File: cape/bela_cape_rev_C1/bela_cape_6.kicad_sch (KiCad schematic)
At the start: 42 parts, among them IC3 ES9080Q, U1 TL974, U2 TL974

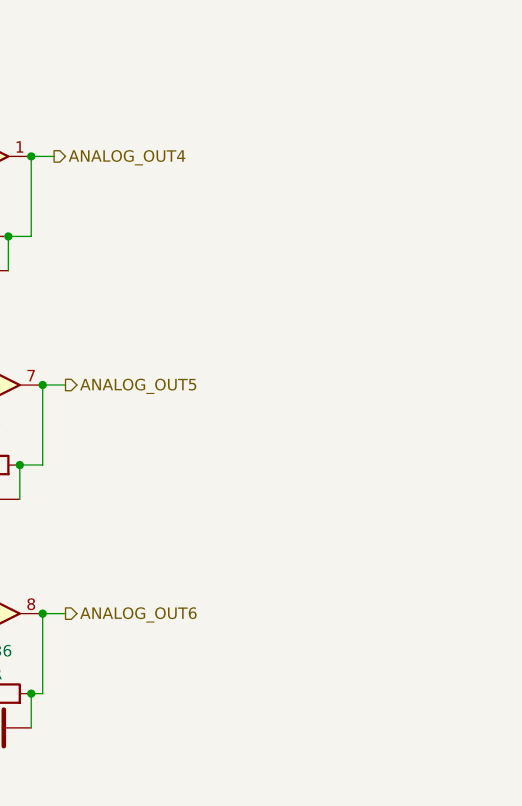
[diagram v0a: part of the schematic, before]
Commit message: Updates to Bela cape C1, adding 3-pin connectors for raw analog out
(cherry picked from commit eb88a9ebe73bf9c3f735ce6d0fd609408781e91a)
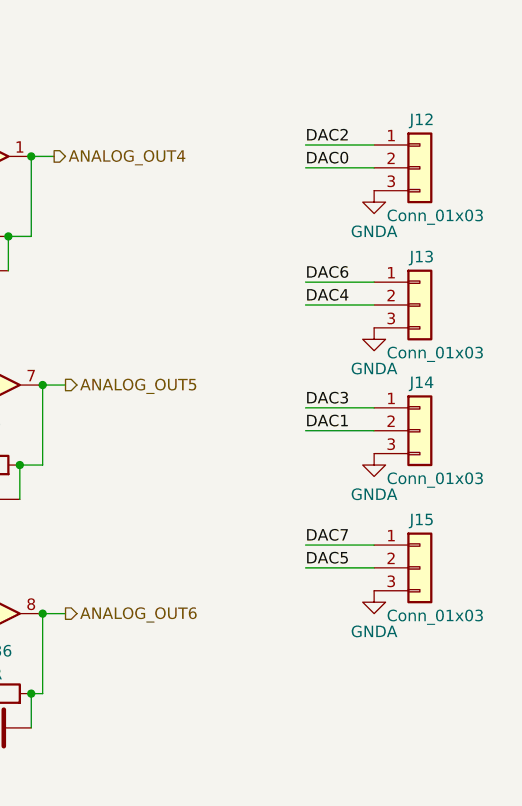
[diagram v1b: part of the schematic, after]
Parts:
- added J12, J13, J14, J15: Conn_01x03, Connector_Molex:Molex_KK-254_AE-6410-03A_1x03_P2.54mm_Vertical, symbol Connector_Generic:Conn_01x03
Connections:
- net DAC0: now also J12.2 (Pin_2)
- net DAC1: now also J14.2 (Pin_2)
- net DAC2: now also J12.1 (Pin_1)
- net DAC3: now also J14.1 (Pin_1)
- net DAC4: now also J13.2 (Pin_2)
- net DAC5: now also J15.2 (Pin_2)
- net DAC6: now also J13.1 (Pin_1)
- net DAC7: now also J15.1 (Pin_1)
- net GNDA: now also J12.3 (Pin_3), J13.3 (Pin_3), J14.3 (Pin_3), J15.3 (Pin_3)
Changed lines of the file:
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@@
   (junction (at 198.12 82.55) (diameter 0) (color 0 0 0 0)
   )
+  (wire (pts (xy 227.33 77.47) (xy 234.95 77.47))
+    (stroke (width 0) (type default) (color 0 0 0 0))
+  )
   (wire (pts (xy 83.82 114.3) (xy 83.82 113.03))
     (stroke (width 0) (type default) (color 0 0 0 0))
@@
     (stroke (width 0) (type default) (color 0 0 0 0))
   )
+  (wire (pts (xy 227.33 30.48) (xy 234.95 30.48))
+    (stroke (width 0) (type default) (color 0 0 0 0))
+  )
   (wire (pts (xy 63.5 104.14) (xy 63.5 114.3))
     (stroke (width 0) (type default) (color 0 0 0 0))
@@
     (stroke (width 0) (type default) (color 0 0 0 0))
   )
+  (wire (pts (xy 227.33 59.69) (xy 234.95 59.69))
+    (stroke (width 0) (type default) (color 0 0 0 0))
+  )
   (wire (pts (xy 147.32 59.69) (xy 147.32 66.04))
     (stroke (width 0) (type default) (color 0 0 0 0))
   )
+  (wire (pts (xy 227.33 62.23) (xy 234.95 62.23))
+    (stroke (width 0) (type default) (color 0 0 0 0))
+  )
   (wire (pts (xy 69.85 170.18) (xy 69.85 166.37))
     (stroke (width 0) (type default) (color 0 0 0 0))
@@
     (stroke (width 0) (type default) (color 0 0 0 0))
   )
+  (wire (pts (xy 227.33 74.93) (xy 234.95 74.93))
+    (stroke (width 0) (type default) (color 0 0 0 0))
+  )
   (wire (pts (xy 102.87 83.82) (xy 102.87 85.09))
     (stroke (width 0) (type default) (color 0 0 0 0))
@@
     (stroke (width 0) (type default) (color 0 0 0 0))
   )
+  (wire (pts (xy 227.33 33.02) (xy 234.95 33.02))
+    (stroke (width 0) (type default) (color 0 0 0 0))
+  )
   (wire (pts (xy 73.66 123.19) (xy 66.04 123.19))
     (stroke (width 0) (type default) (color 0 0 0 0))
@@
     (stroke (width 0) (type default) (color 0 0 0 0))
   )
+  (wire (pts (xy 227.33 45.72) (xy 234.95 45.72))
+    (stroke (width 0) (type default) (color 0 0 0 0))
+  )
   (wire (pts (xy 161.29 31.75) (xy 163.83 31.75))
     (stroke (width 0) (type default) (color 0 0 0 0))
@@
   )
   (wire (pts (xy 171.45 118.11) (xy 175.26 118.11))
+    (stroke (width 0) (type default) (color 0 0 0 0))
+  )
+  (wire (pts (xy 227.33 48.26) (xy 234.95 48.26))
     (stroke (width 0) (type default) (color 0 0 0 0))
   )
@@
     (effects (font (size 1.27 1.27)) (justify right bottom))
   )
+  (label "DAC2" (at 227.33 30.48 0)
+    (effects (font (size 1.27 1.27)) (justify left bottom))
+  )
+  (label "DAC1" (at 227.33 62.23 0)
+    (effects (font (size 1.27 1.27)) (justify left bottom))
+  )
   (label "GND_SNS_R" (at 96.52 77.47 0)
     (effects (font (size 1.27 1.27)) (justify left bottom))
@@
     (effects (font (size 1.27 1.27)) (justify left bottom))
   )
+  (label "DAC6" (at 227.33 45.72 0)
+    (effects (font (size 1.27 1.27)) (justify left bottom))
+  )
+  (label "DAC7" (at 227.33 74.93 0)
+    (effects (font (size 1.27 1.27)) (justify left bottom))
+  )
   (label "DAC1" (at 137.16 54.61 0)
     (effects (font (size 1.27 1.27)) (justify left bottom))
@@
     (effects (font (size 1.27 1.27)) (justify left bottom))
   )
+  (label "DAC5" (at 227.33 77.47 0)
+    (effects (font (size 1.27 1.27)) (justify left bottom))
+  )
   (label "PNEG" (at 71.12 114.3 90)
+    (effects (font (size 1.27 1.27)) (justify left bottom))
+  )
+  (label "DAC0" (at 227.33 33.02 0)
+    (effects (font (size 1.27 1.27)) (justify left bottom))
+  )
+  (label "DAC4" (at 227.33 48.26 0)
     (effects (font (size 1.27 1.27)) (justify left bottom))
   )
   (label "DAC6" (at 50.8 82.55 180)
     (effects (font (size 1.27 1.27)) (justify right bottom))
+  )
+  (label "DAC3" (at 227.33 59.69 0)
+    (effects (font (size 1.27 1.27)) (justify left bottom))
   )
   (label "DAC2" (at 137.16 80.01 0)
@@
   (hierarchical_label "VNEG_IN" (shape input) (at 81.28 175.26 0)
     (effects (font (size 1.27 1.27)) (justify left))
+  )
+  (symbol (lib_id "Connector_Generic:Conn_01x03") (at 240.03 77.47 0) (unit 1)
+    (in_bom yes) (on_board yes)
+    (property "Reference" "J15" (id 0) (at 238.887 72.136 0)
+      (effects (font (size 1.27 1.27)) (justify left))
+    )
+    (property "Value" "Conn_01x03" (id 1) (at 236.347 82.804 0)
+      (effects (font (size 1.27 1.27)) (justify left))
+    )
+    (property "Footprint" "Connector_Molex:Molex_KK-254_AE-6410-03A_1x03_P2.54mm_Vertical" (id 2) (at 240.03 77.47 0)
+      (effects (font (size 1.27 1.27)) hide)
+    )
+    (property "Datasheet" "~" (id 3) (at 240.03 77.47 0)
+      (effects (font (size 1.27 1.27)) hide)
+    )
+    (pin "1")
+    (pin "2")
+    (pin "3")
   )
   (symbol (lib_id "Device:C") (at 193.04 95.25 270) (unit 1)
@@
     (pin "4")
   )
+  (symbol (lib_id "power:GNDA") (at 234.95 64.77 0) (unit 1)
+    (in_bom yes) (on_board yes)
+    (property "Reference" "#PWR0101" (id 0) (at 234.95 71.12 0)
+      (effects (font (size 1.27 1.27)) hide)
+    )
+    (property "Value" "GNDA" (id 1) (at 234.95 69.3325 0))
+    (property "Footprint" "" (id 2) (at 234.95 64.77 0)
+      (effects (font (size 1.27 1.27)) hide)
+    )
+    (property "Datasheet" "" (id 3) (at 234.95 64.77 0)
+      (effects (font (size 1.27 1.27)) hide)
+    )
+    (pin "1")
+  )
   (symbol (lib_id "Device:C") (at 44.45 90.17 180) (unit 1)
     (in_bom yes) (on_board yes)
@@
     )
     (pin "1")
+  )
+  (symbol (lib_id "Connector_Generic:Conn_01x03") (at 240.03 62.23 0) (unit 1)
+    (in_bom yes) (on_board yes)
+    (property "Reference" "J14" (id 0) (at 238.887 56.896 0)
+      (effects (font (size 1.27 1.27)) (justify left))
+    )
+    (property "Value" "Conn_01x03" (id 1) (at 236.347 67.564 0)
+      (effects (font (size 1.27 1.27)) (justify left))
+    )
+    (property "Footprint" "Connector_Molex:Molex_KK-254_AE-6410-03A_1x03_P2.54mm_Vertical" (id 2) (at 240.03 62.23 0)
+      (effects (font (size 1.27 1.27)) hide)
+    )
+    (property "Datasheet" "~" (id 3) (at 240.03 62.23 0)
+      (effects (font (size 1.27 1.27)) hide)
+    )
+    (pin "1")
+    (pin "2")
+    (pin "3")
   )
   (symbol (lib_id "Amplifier_Operational:TL074") (at 153.67 31.75 0) (unit 1)
@@
     (pin "1")
   )
+  (symbol (lib_id "power:GNDA") (at 234.95 35.56 0) (unit 1)
+    (in_bom yes) (on_board yes)
+    (property "Reference" "#PWR0104" (id 0) (at 234.95 41.91 0)
+      (effects (font (size 1.27 1.27)) hide)
+    )
+    (property "Value" "GNDA" (id 1) (at 234.95 40.1225 0))
+    (property "Footprint" "" (id 2) (at 234.95 35.56 0)
+      (effects (font (size 1.27 1.27)) hide)
+    )
+    (property "Datasheet" "" (id 3) (at 234.95 35.56 0)
+      (effects (font (size 1.27 1.27)) hide)
+    )
+    (pin "1")
+  )
+  (symbol (lib_id "power:GNDA") (at 234.95 50.8 0) (unit 1)
+    (in_bom yes) (on_board yes)
+    (property "Reference" "#PWR0130" (id 0) (at 234.95 57.15 0)
+      (effects (font (size 1.27 1.27)) hide)
+    )
+    (property "Value" "GNDA" (id 1) (at 234.95 55.3625 0))
+    (property "Footprint" "" (id 2) (at 234.95 50.8 0)
+      (effects (font (size 1.27 1.27)) hide)
+    )
+    (property "Datasheet" "" (id 3) (at 234.95 50.8 0)
+      (effects (font (size 1.27 1.27)) hide)
+    )
+    (pin "1")
+  )
   (symbol (lib_id "Device:R") (at 140.97 91.44 90) (unit 1)
     (in_bom yes) (on_board yes) (fields_autoplaced)
@@
     (pin "4")
   )
+  (symbol (lib_id "Connector_Generic:Conn_01x03") (at 240.03 48.26 0) (unit 1)
+    (in_bom yes) (on_board yes)
+    (property "Reference" "J13" (id 0) (at 238.887 42.926 0)
+      (effects (font (size 1.27 1.27)) (justify left))
+    )
+    (property "Value" "Conn_01x03" (id 1) (at 236.347 53.594 0)
+      (effects (font (size 1.27 1.27)) (justify left))
+    )
+    (property "Footprint" "Connector_Molex:Molex_KK-254_AE-6410-03A_1x03_P2.54mm_Vertical" (id 2) (at 240.03 48.26 0)
+      (effects (font (size 1.27 1.27)) hide)
+    )
+    (property "Datasheet" "~" (id 3) (at 240.03 48.26 0)
+      (effects (font (size 1.27 1.27)) hide)
+    )
+    (pin "1")
+    (pin "2")
+    (pin "3")
+  )
   (symbol (lib_id "Device:R") (at 176.53 40.64 90) (unit 1)
     (in_bom yes) (on_board yes) (fields_autoplaced)
@@
     (pin "2")
   )
+  (symbol (lib_id "power:GNDA") (at 234.95 80.01 0) (unit 1)
+    (in_bom yes) (on_board yes)
+    (property "Reference" "#PWR0103" (id 0) (at 234.95 86.36 0)
+      (effects (font (size 1.27 1.27)) hide)
+    )
+    (property "Value" "GNDA" (id 1) (at 234.95 84.5725 0))
+    (property "Footprint" "" (id 2) (at 234.95 80.01 0)
+      (effects (font (size 1.27 1.27)) hide)
+    )
+    (property "Datasheet" "" (id 3) (at 234.95 80.01 0)
+      (effects (font (size 1.27 1.27)) hide)
+    )
+    (pin "1")
+  )
   (symbol (lib_id "Device:C") (at 50.8 57.15 0) (unit 1)
     (in_bom yes) (on_board yes)
@@
     (pin "2")
   )
+  (symbol (lib_id "Connector_Generic:Conn_01x03") (at 240.03 33.02 0) (unit 1)
+    (in_bom yes) (on_board yes)
+    (property "Reference" "J12" (id 0) (at 238.887 27.686 0)
+      (effects (font (size 1.27 1.27)) (justify left))
+    )
+    (property "Value" "Conn_01x03" (id 1) (at 236.347 38.354 0)
+      (effects (font (size 1.27 1.27)) (justify left))
+    )
+    (property "Footprint" "Connector_Molex:Molex_KK-254_AE-6410-03A_1x03_P2.54mm_Vertical" (id 2) (at 240.03 33.02 0)
+      (effects (font (size 1.27 1.27)) hide)
+    )
+    (property "Datasheet" "~" (id 3) (at 240.03 33.02 0)
+      (effects (font (size 1.27 1.27)) hide)
+    )
+    (pin "1")
+    (pin "2")
+    (pin "3")
+  )
   (symbol (lib_id "Device:R") (at 154.94 91.44 90) (unit 1)

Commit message: More C1 cape routing
(cherry picked from commit db7d999e21b46c22925661ce0002776775f31ffd)
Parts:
- added JP1: SolderJumper_2_Bridged, Jumper:SolderJumper-2_P1.3mm_Bridged_Pad1.0x1.5mm, symbol Jumper:SolderJumper_2_Bridged
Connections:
- net ANALOG_OUT1: now also C33.1, R27.2, U1.8; no longer C32.1, R26.2, U1.7
- net ANALOG_OUT2: now also C32.1, R26.2, U1.7; no longer C33.1, R27.2, U1.8
- net ANALOG_OUT5: now also C40.1, R36.2, U2.8; no longer C38.1, R34.2, U2.7
- net ANALOG_OUT6: now also C38.1, R34.2, U2.7; no longer C40.1, R36.2, U2.8
- net DAC1: now also U1.10 (+); no longer U1.5 (+)
- net DAC2: now also U1.5 (+); no longer U1.10 (+)
- net DAC5: now also U2.10 (+); no longer U2.5 (+)
- net DAC6: now also U2.5 (+); no longer U2.10 (+)
- net PNEG: now also JP1.1 (A); no longer D2.2 (K)
- net GNDD renamed GND
- new net: D2.2 (K), JP1.2 (B)
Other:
- moved on the sheet: C32, C33, C36, C38, C40, C44, R21, R22, R26, R27, R29, R30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
